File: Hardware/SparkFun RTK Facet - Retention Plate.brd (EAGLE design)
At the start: 50 x 24 mm, 9 parts

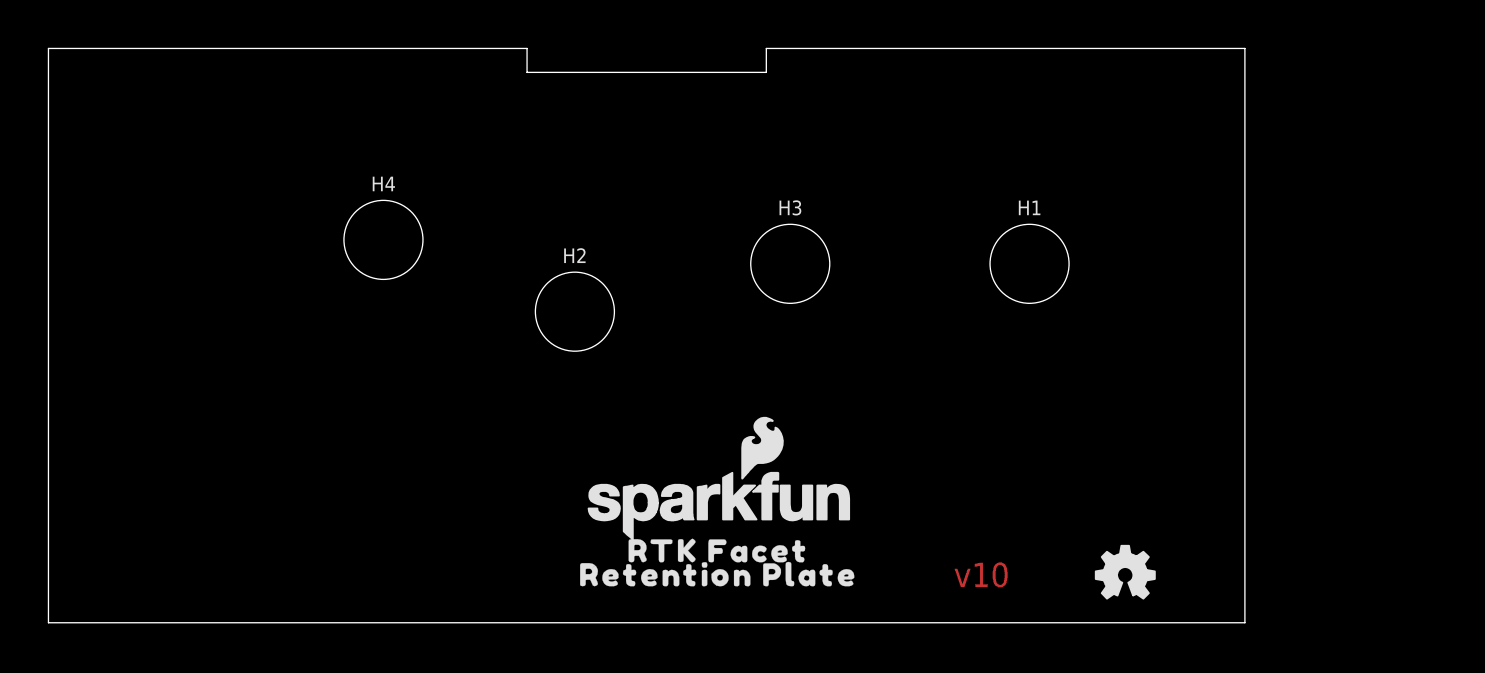
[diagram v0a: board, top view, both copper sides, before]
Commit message: Update Retention Plate design as per current Fusion model
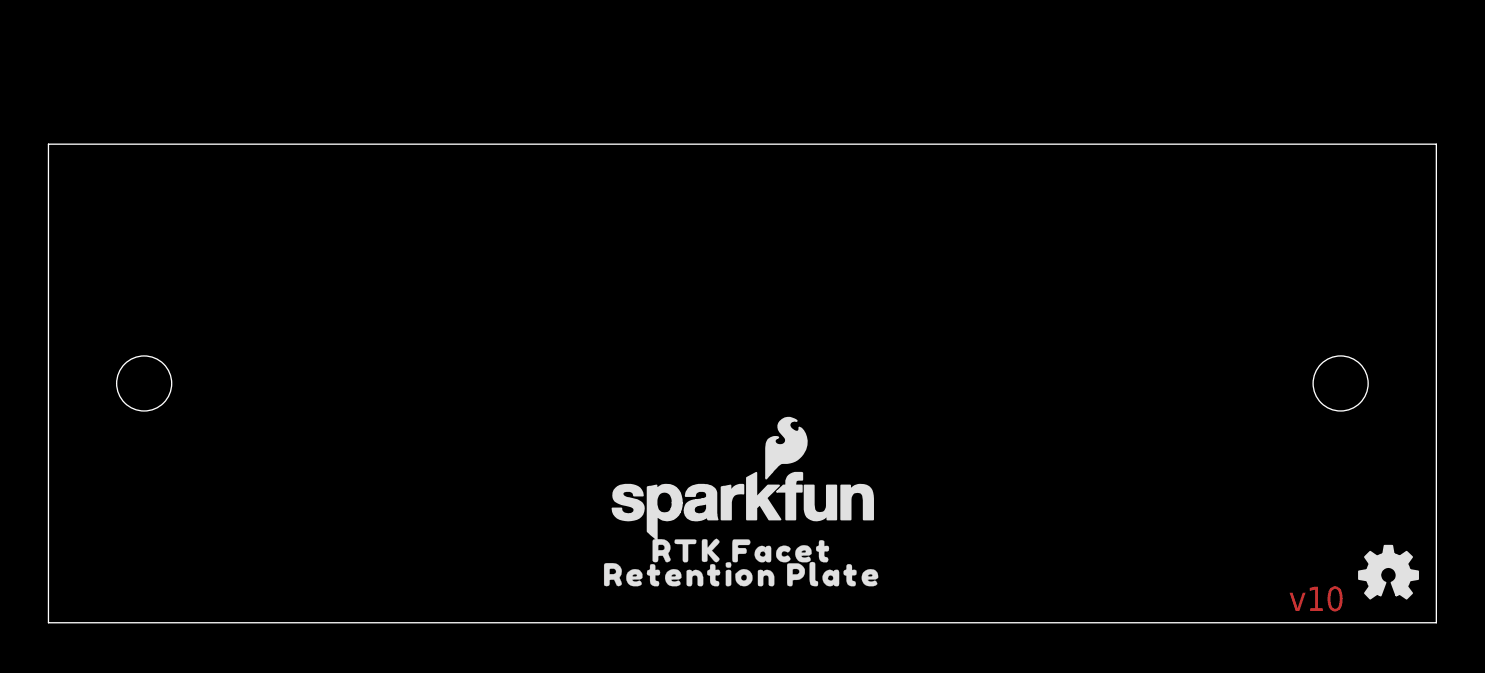
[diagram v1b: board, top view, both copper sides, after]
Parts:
- removed H1, H2, H3, H4: STAND-OFF, SparkFun-Hardware:STAND-OFF
- added U$3: (no value), SparkFun-Aesthetics:ORDERING_INSTRUCTIONS
- moved LOGO3 11.0 mm to (56.0, 2.00)
- moved LOGO5 1.00 mm to (29.1, 4.90)
- moved U$1 1.00 mm to (29.0, 2.00)
- moved U$2 1.00 mm to (29.0, 3.00)
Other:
- board size 50 x 24 mm -> 58 x 20 mm
- board text added: "0.8mm PCB Thickness"
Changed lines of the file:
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@@
 <?xml version="1.0" encoding="utf-8"?>
 <!DOCTYPE eagle SYSTEM "eagle.dtd">
-<eagle version="9.6.2">
+<eagle version="9.5.2">
 <drawing>
 <settings>
@@
 <setting verticaltext="up"/>
 </settings>
-<grid distance="1" unitdist="mm" unit="mm" style="lines" multiple="1" display="yes" altdistance="0.1" altunitdist="mm" altunit="mm"/>
+<grid distance="0.05" unitdist="inch" unit="inch" style="lines" multiple="1" display="yes" altdistance="0.005" altunitdist="inch" altunit="inch"/>
 <layers>
 <layer number="1" name="Top" color="4" fill="1" visible="yes" active="yes"/>
@@
 <layer number="23" name="tOrigins" color="15" fill="1" visible="yes" active="yes"/>
 <layer number="24" name="bOrigins" color="15" fill="1" visible="yes" active="yes"/>
-<layer number="25" name="tNames" color="7" fill="1" visible="yes" active="yes"/>
-<layer number="26" name="bNames" color="7" fill="1" visible="yes" active="yes"/>
-<layer number="27" name="tValues" color="7" fill="1" visible="yes" active="yes"/>
-<layer number="28" name="bValues" color="7" fill="1" visible="yes" active="yes"/>
-<layer number="29" name="tStop" color="7" fill="3" visible="yes" active="yes"/>
-<layer number="30" name="bStop" color="7" fill="6" visible="yes" active="yes"/>
-<layer number="31" name="tCream" color="7" fill="4" visible="yes" active="yes"/>
-<layer number="32" name="bCream" color="7" fill="5" visible="yes" active="yes"/>
-<layer number="33" name="tFinish" color="6" fill="3" visible="yes" active="yes"/>
-<layer number="34" name="bFinish" color="6" fill="6" visible="yes" active="yes"/>
-<layer number="35" name="tGlue" color="7" fill="4" visible="yes" active="yes"/>
-<layer number="36" name="bGlue" color="7" fill="5" visible="yes" active="yes"/>
-<layer number="37" name="tTest" color="7" fill="1" visible="yes" active="yes"/>
-<layer number="38" name="bTest" color="7" fill="1" visible="yes" active="yes"/>
-<layer number="39" name="tKeepout" color="4" fill="11" visible="yes" active="yes"/>
-<layer number="40" name="bKeepout" color="1" fill="11" visible="yes" active="yes"/>
-<layer number="41" name="tRestrict" color="4" fill="10" visible="yes" active="yes"/>
-<layer number="42" name="bRestrict" color="1" fill="10" visible="yes" active="yes"/>
-<layer number="43" name="vRestrict" color="2" fill="10" visible="yes" active="yes"/>
-<layer number="44" name="Drills" color="7" fill="1" visible="yes" active="yes"/>
+<layer number="25" name="tNames" color="7" fill="1" visible="no" active="yes"/>
+<layer number="26" name="bNames" color="7" fill="1" visible="no" active="yes"/>
+<layer number="27" name="tValues" color="7" fill="1" visible="no" active="yes"/>
+<layer number="28" name="bValues" color="7" fill="1" visible="no" active="yes"/>
+<layer number="29" name="tStop" color="7" fill="3" visible="no" active="yes"/>
+<layer number="30" name="bStop" color="7" fill="6" visible="no" active="yes"/>
+<layer number="31" name="tCream" color="7" fill="4" visible="no" active="yes"/>
+<layer number="32" name="bCream" color="7" fill="5" visible="no" active="yes"/>
+<layer number="33" name="tFinish" color="6" fill="3" visible="no" active="yes"/>
+<layer number="34" name="bFinish" color="6" fill="6" visible="no" active="yes"/>
+<layer number="35" name="tGlue" color="7" fill="4" visible="no" active="yes"/>
+<layer number="36" name="bGlue" color="7" fill="5" visible="no" active="yes"/>
+<layer number="37" name="tTest" color="7" fill="1" visible="no" active="yes"/>
+<layer number="38" name="bTest" color="7" fill="1" visible="no" active="yes"/>
+<layer number="39" name="tKeepout" color="4" fill="11" visible="no" active="yes"/>
+<layer number="40" name="bKeepout" color="1" fill="11" visible="no" active="yes"/>
+<layer number="41" name="tRestrict" color="4" fill="10" visible="no" active="yes"/>
+<layer number="42" name="bRestrict" color="1" fill="10" visible="no" active="yes"/>
+<layer number="43" name="vRestrict" color="2" fill="10" visible="no" active="yes"/>
+<layer number="44" name="Drills" color="7" fill="1" visible="no" active="yes"/>
 <layer number="45" name="Holes" color="7" fill="1" visible="yes" active="yes"/>
-<layer number="46" name="Milling" color="3" fill="1" visible="yes" active="yes"/>
-<layer number="47" name="Measures" color="7" fill="1" visible="yes" active="yes"/>
-<layer number="48" name="Document" color="7" fill="1" visible="yes" active="yes"/>
-<layer number="49" name="Reference" color="7" fill="1" visible="yes" active="yes"/>
-<layer number="50" name="dxf" color="7" fill="1" visible="yes" active="yes"/>
+<layer number="46" name="Milling" color="3" fill="1" visible="no" active="yes"/>
+<layer number="47" name="Measures" color="7" fill="1" visible="no" active="yes"/>
+<layer number="48" name="Document" color="7" fill="1" visible="no" active="yes"/>
+<layer number="49" name="Reference" color="7" fill="1" visible="no" active="yes"/>
+<layer number="50" name="dxf" color="7" fill="1" visible="no" active="yes"/>
 <layer number="51" name="tDocu" color="6" fill="1" visible="yes" active="yes"/>
-<layer number="52" name="bDocu" color="7" fill="1" visible="yes" active="yes"/>
+<layer number="52" name="bDocu" color="7" fill="1" visible="no" active="yes"/>
 <layer number="91" name="Nets" color="2" fill="1" visible="no" active="no"/>
 <layer number="92" name="Busses" color="1" fill="1" visible="no" active="no"/>
@@
 <board>
 <plain>
-<text x="39" y="2" size="1.016" layer="1" font="vector" ratio="20" rot="R180" align="center">v10</text>
-<wire x1="50" y1="0" x2="50" y2="24" width="0.05" layer="20"/>
-<wire x1="0" y1="24" x2="0" y2="0" width="0.05" layer="20"/>
-<wire x1="0" y1="0" x2="50" y2="0" width="0.05" layer="20"/>
+<text x="53" y="1" size="1.016" layer="1" font="vector" ratio="20" rot="R180" align="center">v10</text>
 <rectangle x1="0" y1="0" x2="2" y2="22" layer="39"/>
 <rectangle x1="0" y1="0" x2="2" y2="22" layer="40"/>
 <rectangle x1="48" y1="0" x2="50" y2="22" layer="40"/>
 <rectangle x1="48" y1="0" x2="50" y2="22" layer="39"/>
-<wire x1="25" y1="30" x2="25" y2="-1" width="0.05" layer="51"/>
-<wire x1="30" y1="24" x2="50" y2="24" width="0.05" layer="20"/>
-<wire x1="20" y1="24" x2="0" y2="24" width="0.05" layer="20"/>
-<wire x1="20" y1="23" x2="20" y2="24" width="0.05" layer="20"/>
-<wire x1="30" y1="23" x2="30" y2="24" width="0.05" layer="20"/>
-<wire x1="20" y1="23" x2="30" y2="23" width="0.05" layer="20"/>
+<wire x1="29" y1="26" x2="29" y2="-5" width="0.05" layer="51"/>
+<wire x1="0" y1="0" x2="0" y2="20" width="0.05" layer="20"/>
+<wire x1="0" y1="20" x2="58" y2="20" width="0.05" layer="20"/>
+<wire x1="58" y1="20" x2="58" y2="0" width="0.05" layer="20"/>
+<wire x1="58" y1="0" x2="0" y2="0" width="0.05" layer="20"/>
+<hole x="54" y="10" drill="2.3"/>
+<hole x="4" y="10" drill="2.3"/>
+<text x="68.58" y="22.86" size="1.778" layer="51" font="vector" ratio="15">0.8mm PCB Thickness</text>
 </plain>
 <attributes>
@@
 <attribute name="REV" value="" x="-2.57" y="-29.5" size="1.778" layer="27" display="off"/>
 </element>
-<element name="LOGO3" library="SparkFun-Aesthetics" package="OSHW-LOGO-MINI" value="OSHW-LOGOMINI" x="45" y="2" smashed="yes"/>
-<element name="LOGO5" library="SparkFun-Aesthetics" package="SFE_LOGO_NAME_FLAME_.1" value="SFE_LOGO_NAME_FLAME.1_INCH" x="28.1" y="4.9" smashed="yes"/>
-<element name="H1" library="SparkFun-Hardware" package="STAND-OFF" value="STAND-OFF" x="41" y="15" smashed="yes">
-<attribute name="NAME" x="41" y="17.032" size="0.6096" layer="25" font="vector" ratio="20" align="bottom-center"/>
-<attribute name="VALUE" x="41" y="12.968" size="0.6096" layer="27" font="vector" ratio="20" align="top-center"/>
-</element>
-<element name="H2" library="SparkFun-Hardware" package="STAND-OFF" value="STAND-OFF" x="22" y="13" smashed="yes">
-<attribute name="NAME" x="22" y="15.032" size="0.6096" layer="25" font="vector" ratio="20" align="bottom-center"/>
-<attribute name="VALUE" x="22" y="10.968" size="0.6096" layer="27" font="vector" ratio="20" align="top-center"/>
-</element>
-<element name="H3" library="SparkFun-Hardware" package="STAND-OFF" value="STAND-OFF" x="31" y="15" smashed="yes">
-<attribute name="NAME" x="31" y="17.032" size="0.6096" layer="25" font="vector" ratio="20" align="bottom-center"/>
-<attribute name="VALUE" x="31" y="12.968" size="0.6096" layer="27" font="vector" ratio="20" align="top-center"/>
-</element>
-<element name="H4" library="SparkFun-Hardware" package="STAND-OFF" value="STAND-OFF" x="14" y="16" smashed="yes">
-<attribute name="NAME" x="14" y="18.032" size="0.6096" layer="25" font="vector" ratio="20" align="bottom-center"/>
-<attribute name="VALUE" x="14" y="13.968" size="0.6096" layer="27" font="vector" ratio="20" align="top-center"/>
-</element>
-<element name="U$1" library="output" package="RETENTION_PLATE1" value="" x="28" y="2" smashed="yes"/>
-<element name="U$2" library="output" package="RTK_FACET0" value="" x="28" y="3" smashed="yes"/>
+<element name="LOGO3" library="SparkFun-Aesthetics" package="OSHW-LOGO-MINI" value="OSHW-LOGOMINI" x="56" y="2" smashed="yes"/>
+<element name="LOGO5" library="SparkFun-Aesthetics" package="SFE_LOGO_NAME_FLAME_.1" value="SFE_LOGO_NAME_FLAME.1_INCH" x="29.1" y="4.9" smashed="yes"/>
+<element name="U$1" library="output" package="RETENTION_PLATE1" value="" x="29" y="2" smashed="yes"/>
+<element name="U$2" library="output" package="RTK_FACET0" value="" x="29" y="3" smashed="yes"/>
+<element name="U$3" library="SparkFun-Aesthetics" package="ORDERING_INSTRUCTIONS" value="" x="66.04" y="36.83" smashed="yes"/>
 </elements>
 <signals>
